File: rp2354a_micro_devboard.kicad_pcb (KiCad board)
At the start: 2 copper layers, 73 parts, among them J1 BAT+, J2 BAT-, J3 USB_C_Receptacle_USB2.0_16P, J4 01x20_PinHeader_P2.54mm, J5 01x20_PinHeader_P2.54mm, J6 SWD_SH_3p, Q1 AO3407A, Q2 AO3407A, SW1 HX_MINI_MSK12CO2, U1 TMI3112H, U2 MCP73832-2-OT, U4 RP2354A, U5 USBLC6-2SC6, U6 TPS613222ADBV, Y1 YIC 12M10PB

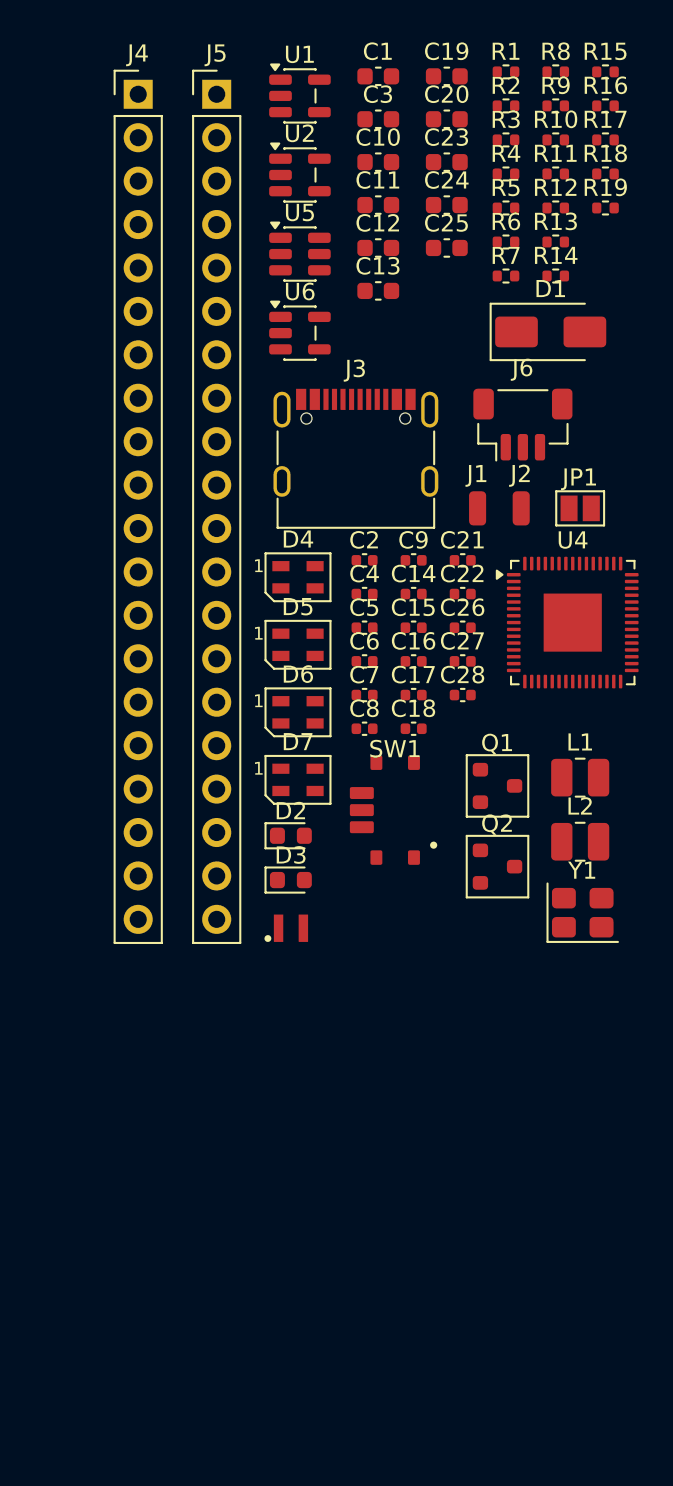
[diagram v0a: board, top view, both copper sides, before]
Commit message: rev0.5の完成とSK6805の削除
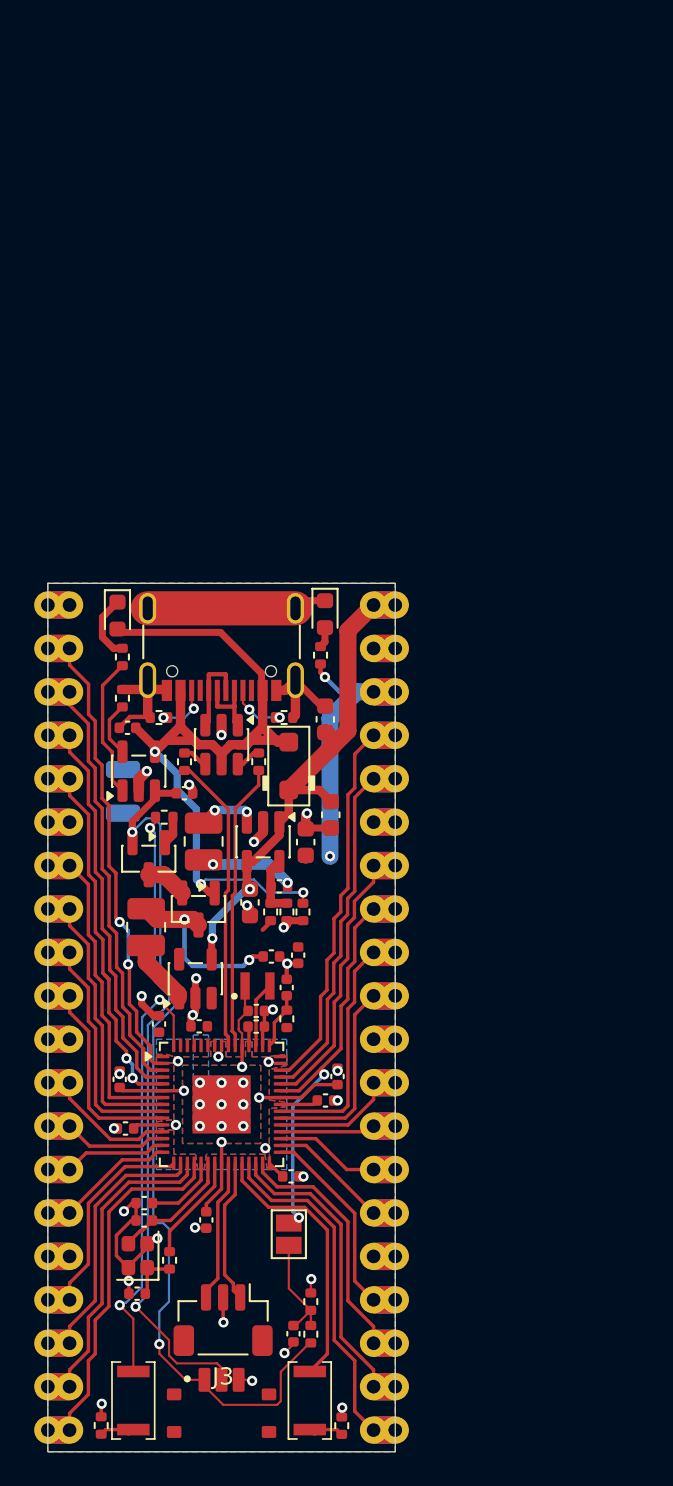
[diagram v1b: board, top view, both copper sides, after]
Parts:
- removed C16, C21, C22: 100n, Capacitor_SMD:C_0402_1005Metric
- removed C20: 4.7u, Capacitor_SMD:C_0603_1608Metric
- removed D2, D3: Red_LED, LED_SMD:LED_0603_1608Metric
- removed D5, D6: SK6805, LED_SMD:LED_SK6805_PLCC4_2.4x2.7mm_P1.3mm
- removed J6: SWD_SH_3p, Connector_JST:JST_SH_BM03B-SRSS-TB_1x03-1MP_P1.00mm_Vertical
- removed R11: 330, Resistor_SMD:R_0402_1005Metric
- removed R13: 1k, Resistor_SMD:R_0402_1005Metric
- removed U6: TPS613222ADBV, Package_TO_SOT_SMD:SOT-23-5
- added SW2: EVPAWCD40, Download_Lib:SW_SPST_EVPAW, F.Cu at (107.9, 120.2)
- added SW3: HX_MINI_MSK12CO2, Download_Lib:HX_MINI_MSK12CO2, F.Cu at (113.0, 120.9)
- added U3: TMI3112H, Package_TO_SOT_SMD:SOT-23-5, F.Cu at (115.5, 87.5)
- C1: value 22u -> 15p; footprint Capacitor_SMD:C_0603_1608Metric -> Capacitor_SMD:C_0402_1005Metric
- C10: value 4.7u -> 15p; footprint Capacitor_SMD:C_0603_1608Metric -> Capacitor_SMD:C_0402_1005Metric
- C12: value 22u -> 100n; footprint Capacitor_SMD:C_0603_1608Metric -> Capacitor_SMD:C_0402_1005Metric
- C13, C19: value 4.7u -> 100n; footprint Capacitor_SMD:C_0603_1608Metric -> Capacitor_SMD:C_0402_1005Metric
- C23, C24, C25: footprint Capacitor_SMD:C_0603_1608Metric -> Capacitor_SMD:C_0402_1005Metric
- C26: value 15p -> 100n
- C27: value 15p -> 22u; footprint Capacitor_SMD:C_0402_1005Metric -> Capacitor_SMD:C_0603_1608Metric
- C28, C5: value 100n -> 22u; footprint Capacitor_SMD:C_0402_1005Metric -> Capacitor_SMD:C_0603_1608Metric
- C3: value 22u -> 4.7u; footprint Capacitor_SMD:C_0603_1608Metric -> Capacitor_SMD:C_0402_1005Metric
- C4, C8, C9: value 100n -> 4.7u
- D1: value SS32 -> SS2040FL; footprint Diode_SMD:D_SMA -> PCM_Diode_SMD_AKL:D_SOD-123F
- D4, D7: value SK6805 -> Red_LED; footprint LED_SMD:LED_SK6805_PLCC4_2.4x2.7mm_P1.3mm -> LED_SMD:LED_0603_1608Metric
- J1: value BAT+ -> USB_C_Receptacle_USB2.0_16P; footprint Connector_Wire:SolderWirePad_1x01_SMD_1x2mm -> Connector_USB:USB_C_Receptacle_G-Switch_GT-USB-7010ASV
- J2: value BAT- -> Micro-DevBoard; footprint Connector_Wire:SolderWirePad_1x01_SMD_1x2mm -> Download_Lib:Micro-DevBoard
- J3: value USB_C_Receptacle_USB2.0_16P -> SWDIO; footprint Connector_USB:USB_C_Receptacle_G-Switch_GT-USB-7010ASV -> Connector_JST:JST_SH_BM03B-SRSS-TB_1x03-1MP_P1.00mm_Vertical
- J4: value 01x20_PinHeader_P2.54mm -> BAT+; footprint Connector_PinHeader_2.54mm:PinHeader_1x20_P2.54mm_Vertical -> Connector_Wire:SolderWirePad_1x01_SMD_1x2mm; moved to B.Cu
- J5: value 01x20_PinHeader_P2.54mm -> BAT-; footprint Connector_PinHeader_2.54mm:PinHeader_1x20_P2.54mm_Vertical -> Connector_Wire:SolderWirePad_1x01_SMD_1x2mm; moved to B.Cu
- L1: value 1uH -> 3.3uH; footprint Inductor_SMD:L_1008_2520Metric -> PCM_SparkFun-Coil:0806_Polarized
- L3: value 3.3uH -> 1uH; footprint PCM_SparkFun-Coil:0806_Polarized -> Inductor_SMD:L_1008_2520Metric
- Q1, Q2: footprint PCM_Package_TO_SOT_SMD_AKL:SOT-23 -> Package_TO_SOT_SMD:SOT-23
- R1, R2: value 5k1 -> 1k
- R10: value 330 -> 33k2
- R12, R15: value 27 -> 5k1
- R14: value 27 -> 150k
- R16: value 1k -> 150k
- R3, R6: value 150k -> 27
- R4: value 5k1 -> 27
- R5: value 150k -> 1k
- R7: value 33k2 -> 5k1
- R8: value 1k -> 5k1
- R9: value 5k1 -> 150k
- SW1: value HX_MINI_MSK12CO2 -> EVPAWCD40; footprint Download_Lib:HX_MINI_MSK12CO2 -> Download_Lib:SW_SPST_EVPAW
- U1: value TMI3112H -> USBLC6-2SC6; footprint Package_TO_SOT_SMD:SOT-23-5 -> Package_TO_SOT_SMD:SOT-23-6
- U2: value MCP73832-2-OT -> RP2354A; footprint Package_TO_SOT_SMD:SOT-23-5 -> Package_DFN_QFN:QFN-60-1EP_7x7mm_P0.4mm_EP3.4x3.4mm
- U4: value RP2354A -> MCP73832-2-OT; footprint Package_DFN_QFN:QFN-60-1EP_7x7mm_P0.4mm_EP3.4x3.4mm -> Package_TO_SOT_SMD:SOT-23-5
- U5: value USBLC6-2SC6 -> TPS613222ADBV; footprint Package_TO_SOT_SMD:SOT-23-6 -> Package_TO_SOT_SMD:SOT-23-5
- Y1: value YIC 12M10PB -> YE12MUBCE2O; footprint Crystal:Crystal_SMD_3225-4Pin_3.2x2.5mm -> Crystal:Crystal_SMD_2016-4Pin_2.0x1.6mm
- moved R2 80.7 mm to (106.0, 121.7), turned to -90 degrees
- moved R1 79.8 mm to (120.1, 121.7), turned to -90 degrees
- moved R18 70.0 mm to (118.2, 116.3), turned to -90 degrees
- moved C1 68.3 mm to (108.5, 109.7)
- moved R19 66.3 mm to (118.2, 114.4), turned to -90 degrees
- moved R5 64.6 mm to (110.0, 112.0), turned to 90 degrees
- moved C19 64.3 mm to (107.4, 104.3), turned to 180 degrees
- moved U2 54.6 mm to (113.0, 102.9)
- moved C3 53.6 mm to (115.1, 98.3), turned to 180 degrees
- moved J3 50.7 mm to (113.1, 115.5), turned to 180 degrees
- moved R16 50.4 mm to (117.8, 91.6), turned to -90 degrees
- moved R9 50.0 mm to (115.9, 91.6), turned to -90 degrees
- moved R10 47.8 mm to (116.8, 91.6), turned to -90 degrees
- moved R6 47.2 mm to (116.8, 97.9), turned to 90 degrees
- moved C12 46.7 mm to (111.7, 98.3), turned to 180 degrees
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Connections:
- C1 pad 1: IO_VBUS -> GND
- C1 pad 2: GND -> Net-(U2-XIN)
- C10 pad 1: Net-(Q2-D) -> Net-(U3-FB)
- C10 pad 2: GND -> +3V3
- C11 pad 1: IO_VBUS -> +3V3
- C12 pad 1: IO_VBUS -> +3V3
- C13 pad 1: GND -> +3V3
- C13 pad 2: USB_VBUS -> GND
- C14 pad 1: GND -> +3V3
- C14 pad 2: IO_VBUS -> GND
- C15 pad 1: GND -> +3V3
- C15 pad 2: IO_VBUS -> GND
- C17 pad 1: GND -> +3V3
- C17 pad 2: IO_VBUS -> GND
- C18 pad 1: Net-(U4-VREG_FB) -> +3V3
- C19 pad 1: BAT_CELL -> +3V3
- C19 pad 2: Net-(C19-Pad2) -> GND
- C2 pad 1: Net-(U1-FB) -> GND
- C2 pad 2: +3V3 -> Net-(C2-Pad2)
- C23 pad 1: Net-(U4-VREG_FB) -> GND
- C23 pad 2: GND -> USB_VBUS
- C24 pad 1: GND -> Net-(Q2-D)
- C24 pad 2: Net-(U4-VREG_AVDD) -> GND
- C25 pad 1: Net-(U4-VREG_FB) -> BAT_CELL
- C26 pad 1: GND -> Net-(JP1-A)
- C26 pad 2: Net-(U4-XIN) -> GND
- C27 pad 1: GND -> IO_VBUS
- C27 pad 2: Net-(C27-Pad2) -> GND
- C28 pad 1: Net-(JP1-A) -> IO_VBUS
- C3 pad 1: +3V3 -> GND
- C3 pad 2: Net-(C3-Pad2) -> +3V3
- C4 pad 1: +3V3 -> GND
- C4 pad 2: Net-(C3-Pad2) -> Net-(U2-VREG_AVDD)
- C5 pad 1: +3V3 -> IO_VBUS
- C5 pad 2: Net-(C3-Pad2) -> GND
- C6 pad 1: +3V3 -> +1V1
- C6 pad 2: Net-(C3-Pad2) -> GND
- C7 pad 1: +3V3 -> +1V1
- C7 pad 2: Net-(C3-Pad2) -> GND
- C8 pad 1: +3V3 -> +1V1
- C8 pad 2: Net-(C3-Pad2) -> GND
- C9 pad 1: +3V3 -> +1V1
- C9 pad 2: Net-(C3-Pad2) -> GND
- D4 pad 1: Net-(D4-DOUT) -> GND
- D4 pad 2: GND -> Net-(D4-A)
- D7 pad 1: Net-(D7-DOUT) -> Net-(D7-K)
- D7 pad 2: GND -> USB_VBUS
- J4 pad 1: GND -> BAT_CELL
- J5 pad 1: IO_VBUS -> GND
- L1 pad 1: Net-(U1-LX) -> +1V1
- L1 pad 2: +3V3 -> Net-(U2-VREG_LX)
- L2 pad 1: Net-(Q2-D) -> Net-(U3-LX)
- L2 pad 2: Net-(U6-SW) -> +3V3
- L3 pad 1: Net-(U4-VREG_LX) -> Net-(Q2-D)
- L3 pad 2: Net-(U4-VREG_FB) -> Net-(U5-SW)
- R1 pad 1: Net-(D2-A) -> GND
- R1 pad 2: +3V3 -> Net-(R1-Pad2)
- R10 pad 1: GPIO6 -> Net-(U3-FB)
- R10 pad 2: Net-(D4-DIN) -> GND
- R12 pad 1: +3V3 -> Net-(D4-A)
- R12 pad 2: Net-(U4-VREG_AVDD) -> +3V3
- R14 pad 1: Net-(U4-USB_DM) -> Net-(Q1-G)
- R14 pad 2: Net-(R14-Pad2) -> Net-(SW3-B)
- R15 pad 1: Net-(U4-USB_DP) -> GND
- R15 pad 2: Net-(R15-Pad2) -> Net-(U4-PROG)
- R16 pad 1: GND -> USB_VBUS
- R16 pad 2: Net-(SW3-A) -> GND
- R17 pad 1: Net-(C27-Pad2) -> Net-(D7-K)
- R17 pad 2: Net-(U4-XOUT) -> Net-(U4-STAT)
- R2 pad 2: Net-(J3-CC1) -> Net-(R2-Pad2)
- R3 pad 1: Net-(U1-FB) -> Net-(U2-USB_DM)
- R3 pad 2: +3V3 -> Net-(R3-Pad2)
- R4 pad 1: GND -> Net-(U2-USB_DP)
- R4 pad 2: Net-(J3-CC2) -> Net-(R4-Pad2)
- R5 pad 1: Net-(Q1-G) -> Net-(C2-Pad2)
- R5 pad 2: Net-(SW1-B) -> Net-(U2-XOUT)
- R6 pad 1: USB_VBUS -> +3V3
- R6 pad 2: GND -> Net-(U2-VREG_AVDD)
- R7 pad 1: Net-(U1-FB) -> GND
- R7 pad 2: GND -> Net-(J1-CC1)
- R8 pad 1: Net-(D3-K) -> GND
- R8 pad 2: Net-(U2-V_{BAT}) -> Net-(J1-CC2)
- R9 pad 1: Net-(C19-Pad2) -> Net-(U3-FB)
- R9 pad 2: Net-(U2-PROG) -> +3V3
- SW1 pad 1: BAT_CELL -> Net-(R1-Pad2)
- SW1 pad 2: Net-(SW1-B) -> Net-(U2-RUN)
- U1 pad 1: IO_VBUS -> D-
- U1 pad 3: Net-(U1-LX) -> D+
- U1 pad 4: IO_VBUS -> Net-(R4-Pad2)
- U1 pad 5: Net-(U1-FB) -> USB_VBUS
- U2 pad 1: BAT_CELL -> +3V3
- U2 pad 2: GND -> GPIO0
- U2 pad 3: Net-(U2-V_{BAT}) -> GPIO1
- U2 pad 4: USB_VBUS -> GPIO2
- U2 pad 5: Net-(U2-PROG) -> GPIO3
- U4 pad 1: +3V3 -> Net-(U4-STAT)
- U4 pad 2: GPIO0 -> GND
- U4 pad 3: GPIO1 -> BAT_CELL
- U4 pad 4: GPIO2 -> USB_VBUS
- U4 pad 5: GPIO3 -> Net-(U4-PROG)
- U5 pad 1: D- -> Net-(U5-SW)
- U5 pad 3: D+ -> unconnected-(U5-NC-Pad3)
- U5 pad 4: Net-(R15-Pad2) -> IO_VBUS
- U5 pad 5: USB_VBUS -> unconnected-(U5-NC-Pad5)
- Y1 pad 1: Net-(C27-Pad2) -> Net-(C2-Pad2)
- Y1 pad 3: Net-(U4-XIN) -> Net-(U2-XIN)
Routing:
- net GND: track 0.00 -> 64.5 mm, vias 0 -> 36
- net BAT_CELL: track 0.00 -> 53.6 mm, vias 0 -> 2
- net USB_VBUS: track 0.00 -> 50.7 mm, vias 0 -> 3
- net Net-(SW3-B): track 0.00 -> 37.8 mm, vias 0 -> 2
- net +3V3: track 0.00 -> 33.7 mm, vias 0 -> 9
- net IO_VBUS: track 0.00 -> 29.2 mm, vias 0 -> 2
- net GPIO0: track 0.00 -> 26.8 mm, vias 0 -> 2
- net Net-(U2-~{QSPI_SS}): track 0.00 -> 26.2 mm, vias 0 -> 2
- net GPIO1: track 0.00 -> 24.8 mm
- net GPIO26: track 0.00 -> 23.2 mm, vias 0 -> 2
- net GPIO2: track 0.00 -> 22.8 mm
- net GPIO29: track 0.00 -> 22.1 mm
- net GPIO3: track 0.00 -> 21.3 mm, vias 0 -> 2
- net GPIO15: track 0.00 -> 20.4 mm
- net GPIO28: track 0.00 -> 20.1 mm
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- added copper zone on B.Cu, net +1V1
- added copper zone on F.Cu, net +1V1
- added copper zone on B.Cu, net +3V3
- added copper zone on F.Cu, net +3V3
- added copper zone on B.Cu, net GND
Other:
- board outline added: 20.3 x 50.8 mm
- board text added: "SW2"

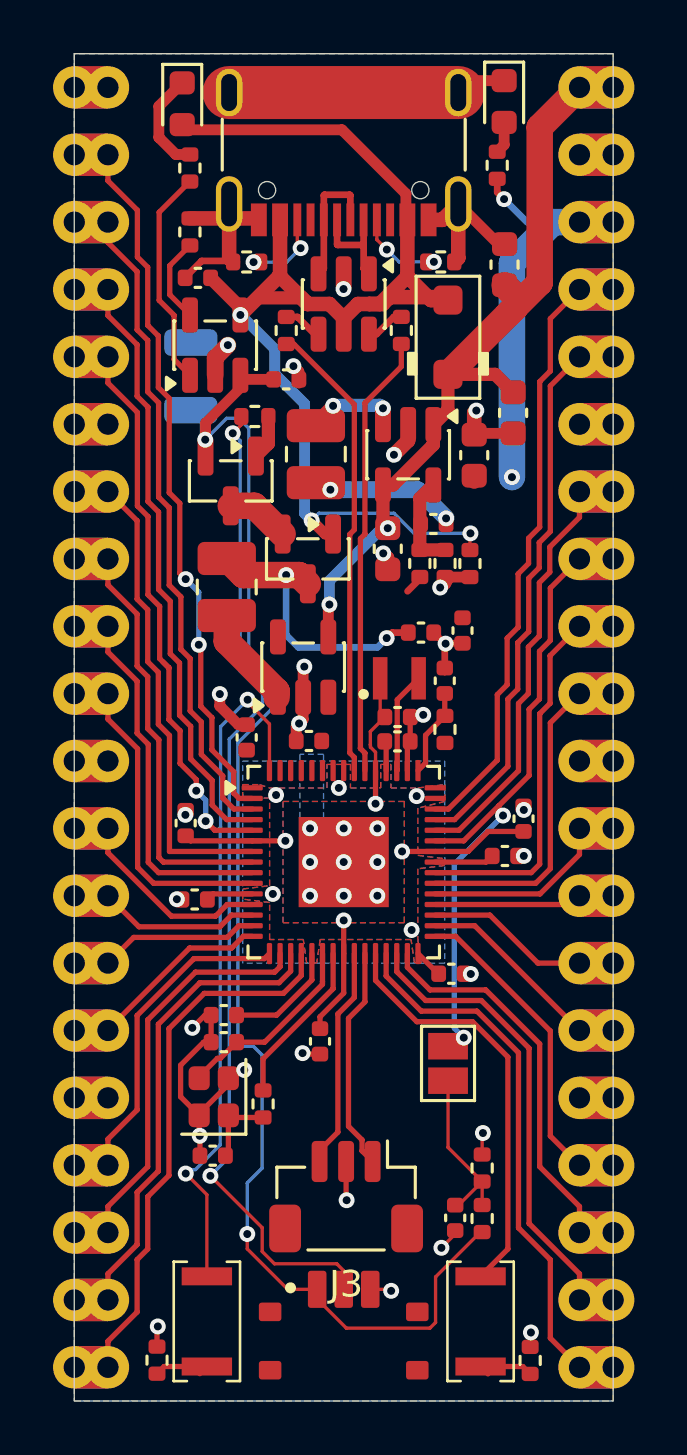
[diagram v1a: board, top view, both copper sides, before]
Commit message: fix: TPS613222 after diode OR cir
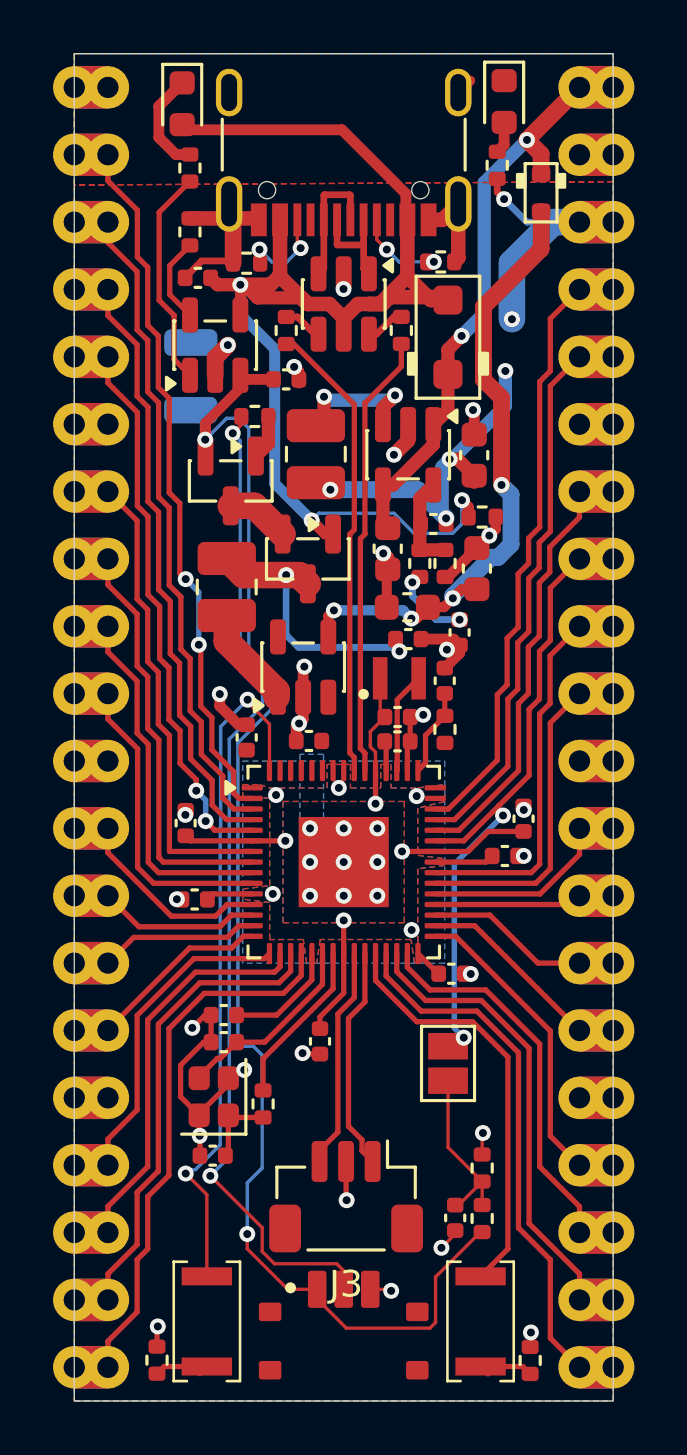
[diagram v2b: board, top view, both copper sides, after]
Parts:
- added D2: RB521S-30, PCM_Diode_SMD_AKL:D_SOD-523, F.Cu at (120.5, 77.6)
- moved C28 11.5 mm to (118.0, 91.8)
- moved C27 8.35 mm to (115.4, 93.3), turned to 180 degrees
- moved R16 1.81 mm to (118.2, 89.9), turned to 0 degrees
- moved C24 0.54 mm to (115.5, 94.5)
- moved C17 0.13 mm to (117.4, 94.2)
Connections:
- C27 pad 1: IO_VBUS -> Net-(D2-A)
- C28 pad 1: IO_VBUS -> Net-(D2-A)
- U5 pad 4: IO_VBUS -> Net-(D2-A)
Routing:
- net Net-(D2-A): track 0.00 -> 24.0 mm, vias 0 -> 4
- net GND: track 64.5 -> 55.6 mm
- net IO_VBUS: track 29.2 -> 21.5 mm
- net +3V3: track 33.7 -> 38.0 mm, vias 9 -> 13
- net USB_VBUS: track 50.7 -> 52.6 mm
- net Net-(U3-LX): track 3.57 -> 5.31 mm
- added copper zone on F.Cu, net GND
